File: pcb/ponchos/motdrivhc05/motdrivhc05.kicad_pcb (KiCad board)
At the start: 2 copper layers, 53.3 x 61.6 mm, 21 parts, among them J1 Screw_Terminal_1x06, J3 GW-040, J4 CONN_01X02, Q1 TIP31, U1 L293

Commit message: Agregado y modificado de nombres de nets en esquemático. Agregado de serigrafías con referencias en PCB.
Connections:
- net /M3A renamed /3A
- net /M4A renamed /4A
- net Net-(D2-Pad2) renamed /M1B
- net Net-(D4-Pad2) renamed /M2B
- net Net-(D9-Pad1) renamed /EXT
- D1 pad 2: Net-(D1-Pad2) -> /M1A
- D3 pad 2: Net-(D3-Pad2) -> /M2A
- D5 pad 1: Net-(D1-Pad2) -> /M1A
- D7 pad 1: Net-(D3-Pad2) -> /M2A
- J1 pad 4: Net-(D1-Pad2) -> /M1A
- J1 pad 6: Net-(D3-Pad2) -> /M2A
- SH1 pad 11: /M2A -> /2A
- SH1 pad 8: /M1A -> /1A
- U1 pad 11: Net-(D3-Pad2) -> /M2A
- U1 pad 2: /M1A -> /1A
- U1 pad 3: Net-(D1-Pad2) -> /M1A
- U1 pad 7: /M2A -> /2A
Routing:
- net /2A: track 0.00 -> 55.6 mm, vias 0 -> 2
- net /1A: track 0.00 -> 54.8 mm, vias 0 -> 2
- net Net-(D1-Pad2): track 46.9 -> 0.00 mm
- net Net-(D3-Pad2): track 38.7 -> 0.00 mm
- net /M2A: track 55.6 -> 38.7 mm, vias 2 -> 0
- net /M1A: track 54.8 -> 46.9 mm, vias 2 -> 0
- net GND: track 270.8 -> 270.1 mm
- net VCC: track 100.5 -> 100.0 mm
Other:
- board text added: "EXT"
- board text added: "GND"
- board text added: "M1A"
- board text added: "M1B"
- board text added: "M2A"
- board text added: "M2B"
- board text added: "NC"
- board text added: "VCC"

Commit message: Corregido error en disposición de pines de módulo bluetooth, y correción en PCB.
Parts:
- moved J3 12.7 mm to (66.7, 77.2)
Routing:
- net /BT_TXD: track 25.3 -> 39.3 mm
- net /BT_STATE: track 10.8 -> 20.6 mm
- net GND: track 270.1 -> 275.9 mm
- net +5V: track 165.9 -> 171.1 mm
- net Net-(J3-Pad2): track 7.27 -> 10.5 mm
- net /2A: track 55.6 -> 54.7 mm

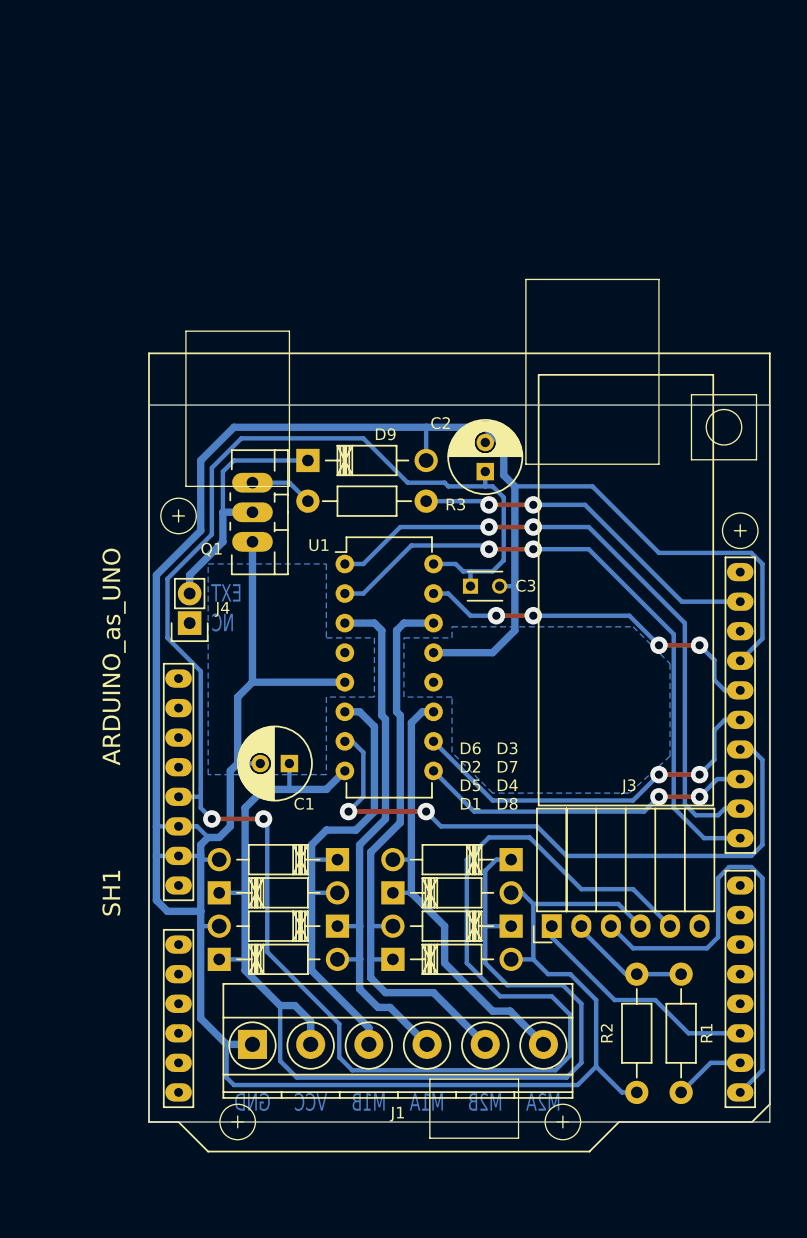
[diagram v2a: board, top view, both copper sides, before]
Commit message: Desplazadas pineras shield arduino. Agregado de serigrafía en capa cobre de datos de laboratorio y versión de la placa. Corregido 3D shape del conector de bluetooth.
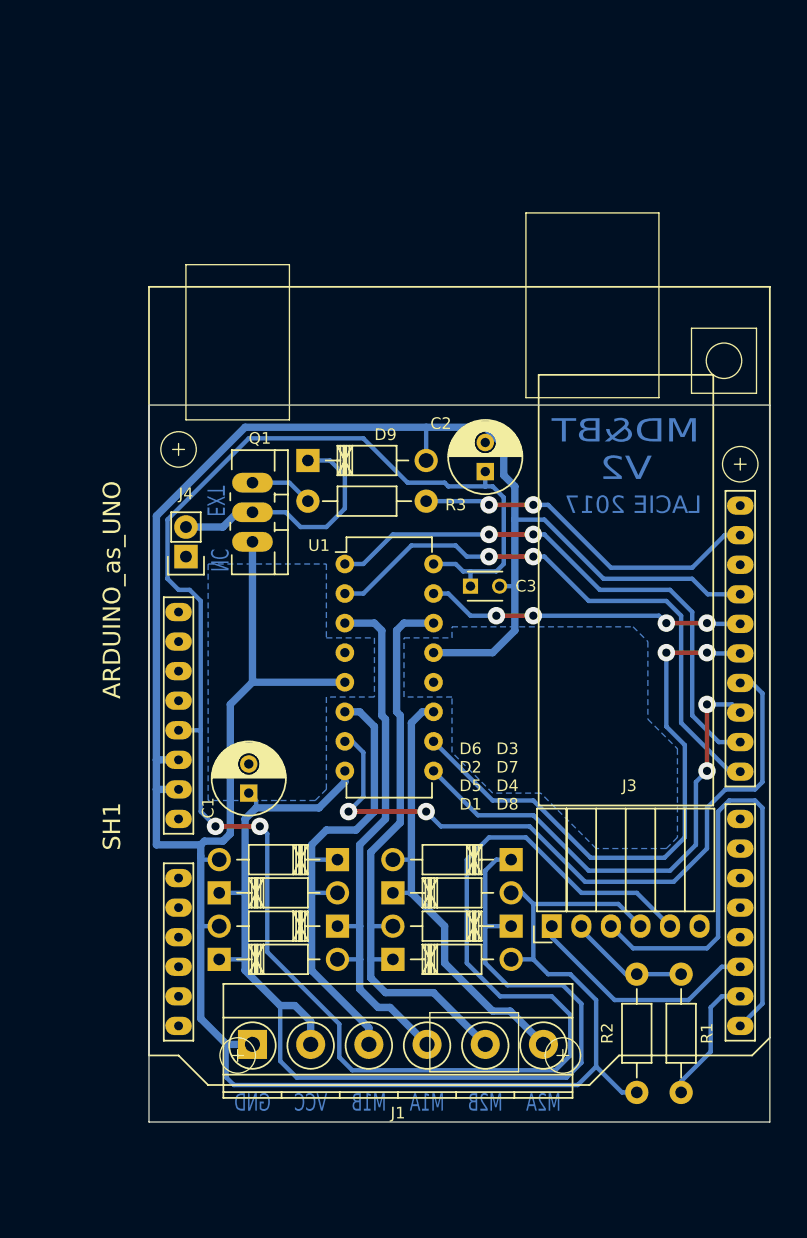
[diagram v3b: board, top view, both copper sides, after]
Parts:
- moved J4 5.72 mm to (35.2, 45.4)
- moved SH1 5.71 mm to (58.7, 56.5)
- moved C1 4.32 mm to (40.6, 65.7), turned to 90 degrees
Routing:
- net GND: track 275.9 -> 252.7 mm
- net /3A: track 32.8 -> 49.4 mm
- net /ME34: track 29.0 -> 42.6 mm
- net /ME12: track 54.9 -> 47.6 mm
- net /2A: track 54.7 -> 61.1 mm
- net /BT_TXD: track 39.3 -> 45.2 mm
- net /1A: track 54.8 -> 49.1 mm
- net /BT_RXD: track 6.13 -> 11.3 mm
- net /4A: track 30.8 -> 27.4 mm
- net VCC: track 100.0 -> 99.3 mm
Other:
- board text added: "LACIE 2017"
- board text added: "MD&BT V2"

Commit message: Algunas correciones varias. Desplazamiento del conector de motores, para que no interfieran las soldaduras con el conector SPI de arduino.
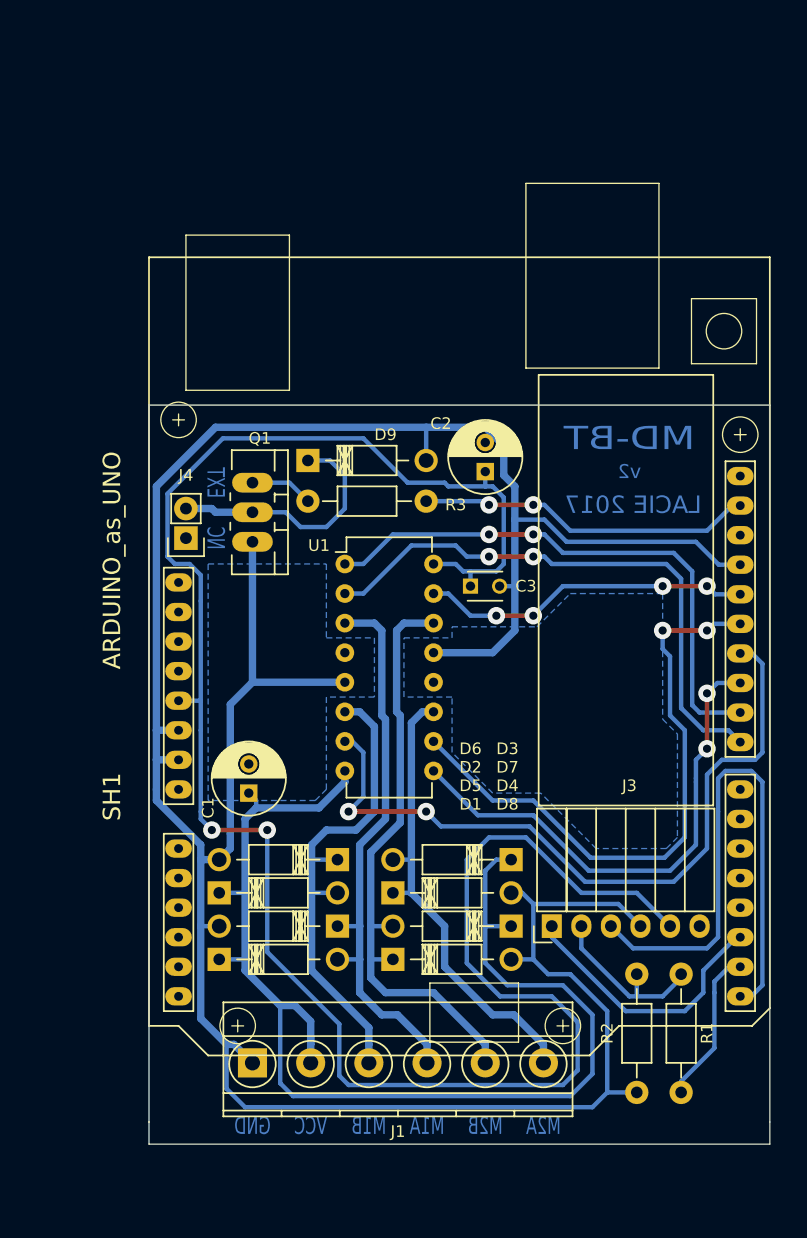
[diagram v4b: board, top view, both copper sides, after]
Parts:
- moved SH1 2.54 mm to (58.7, 54.0)
- moved J1 1.59 mm to (41.0, 88.9)
- moved J4 1.59 mm to (35.2, 43.8)
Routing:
- net VCC: track 99.3 -> 105.2 mm
- net +5V: track 171.1 -> 176.7 mm
- net Net-(J3-Pad2): track 10.5 -> 15.4 mm
- net /BT_TXD: track 45.2 -> 48.3 mm
- net /BT_STATE: track 20.6 -> 23.5 mm
- net /3A: track 49.4 -> 52.3 mm
- net /2A: track 61.1 -> 63.9 mm
- net /BT_RXD: track 11.3 -> 13.5 mm
- net /M1A: track 46.9 -> 48.6 mm
- net /M2A: track 38.7 -> 40.5 mm
- net /M2B: track 50.5 -> 52.1 mm
- net /M1B: track 40.6 -> 42.2 mm
- net /T1: track 30.5 -> 29.0 mm
- net /4A: track 27.4 -> 28.9 mm
- net GND: track 252.7 -> 253.8 mm
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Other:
- board size 53.3 x 61.6 mm -> 53.3 x 63.5 mm
- net class Default: via_dia 1 -> 1.5
- net class Motor: via_dia 1 -> 1.5
- board text added: "MD-BT"
- board text added: "v2"
- board text removed: "MD&BT V2"

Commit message: Corrimiento del conector, agujeros para disipador, giro capacitores para poner acostados, cambio pin del key/status, se quitó el transistor para rele.
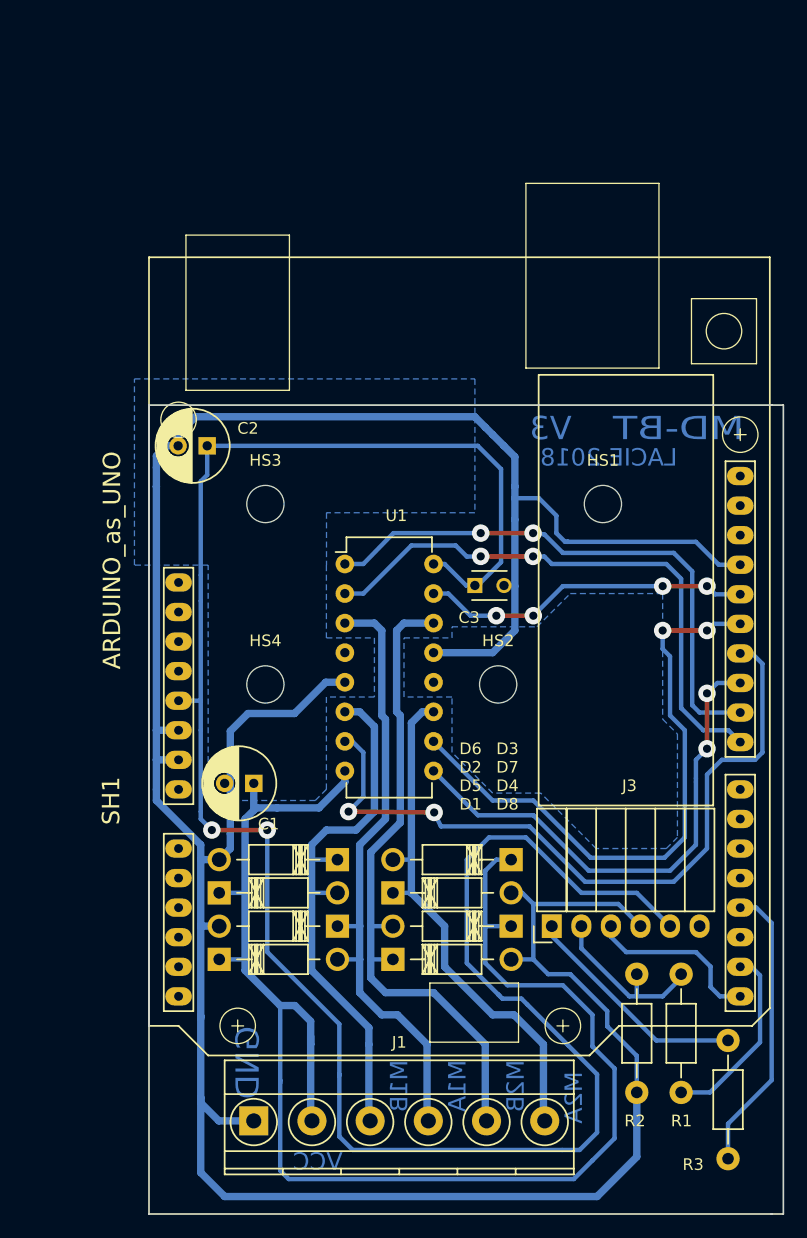
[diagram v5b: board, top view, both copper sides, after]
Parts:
- removed D9: 1N5819, Diodes_ThroughHole:Diode_DO-41_SOD81_Horizontal_RM10
- removed J4: CONN_01X02, Pin_Headers:Pin_Header_Straight_1x02
- removed Q1: TIP31, TO_SOT_Packages_THT:TO-220_Neutral123_Vertical_LargePads
- added HS1: Heatsink_PAD, Mounting_Holes:MountingHole_3.2mm_M3_ISO14580, F.Cu at (71.1, 40.9)
- added HS2: Heatsink_PAD, Mounting_Holes:MountingHole_3.2mm_M3_ISO14580, F.Cu at (62.1, 56.4)
- added HS3: Heatsink_PAD, Mounting_Holes:MountingHole_3.2mm_M3_ISO14580, F.Cu at (42.1, 40.9)
- added HS4: Heatsink_PAD, Mounting_Holes:MountingHole_3.2mm_M3_ISO14580, F.Cu at (42.1, 56.4)
- R3: value 1K -> 2K
- moved R3 67.0 mm to (81.8, 97.1), turned to 90 degrees
- moved C2 24.0 mm to (37.1, 35.9), turned to 180 degrees
- moved J1 4.99 mm to (41.1, 93.9)
- moved C1 0.94 mm to (41.1, 64.9), turned to 180 degrees
- moved C3 0.38 mm to (60.1, 47.9)
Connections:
- net /T2 renamed Net-(SH1-PadA5/2)
- J3 pad 1: /BT_STATE -> Net-(J3-Pad1)
- R3 pad 1: Net-(Q1-Pad1) -> /BT_STATE
- R3 pad 2: /T1 -> Net-(J3-Pad1)
- SH1 pad 2: /BT_STATE -> Net-(SH1-Pad2)
- SH1 pad 3: Net-(SH1-Pad3) -> /BT_STATE
- SH1 pad A4/2: /T1 -> Net-(SH1-PadA4/2)
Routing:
- net /BT_TXD: track 48.3 -> 15.2 mm
- net /T1: track 29.0 -> 0.00 mm, vias 2 -> 0
- net VCC: track 105.2 -> 127.8 mm
- net /EXT: track 21.5 -> 0.00 mm
- net Net-(J3-Pad1): track 0.00 -> 19.7 mm
- net +5V: track 176.7 -> 185.5 mm
- net GND: track 253.8 -> 261.2 mm
- net Net-(Q1-Pad1): track 5.42 -> 0.00 mm
- net /M2A: track 40.5 -> 45.5 mm
- net /M1A: track 48.6 -> 53.7 mm
- net /M1B: track 42.2 -> 47.2 mm
- net /M2B: track 52.1 -> 57.1 mm
- net /BT_RXD: track 13.5 -> 16.3 mm
- net /BT_STATE: track 23.5 -> 25.1 mm
- net Net-(SH1-PadA4/2): track 0.00 -> 0.76 mm
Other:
- board size 53.3 x 63.5 mm -> 54.5 x 69.5 mm
- board text added: "LACIE 2018"
- board text added: "V3"
- board text removed: "EXT"
- board text removed: "LACIE 2017"
- board text removed: "NC"
- board text removed: "v2"

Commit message: Subo el margen de 0,2 a 0,4 y corrijo algunas distancias. Faltan unas pocas más.
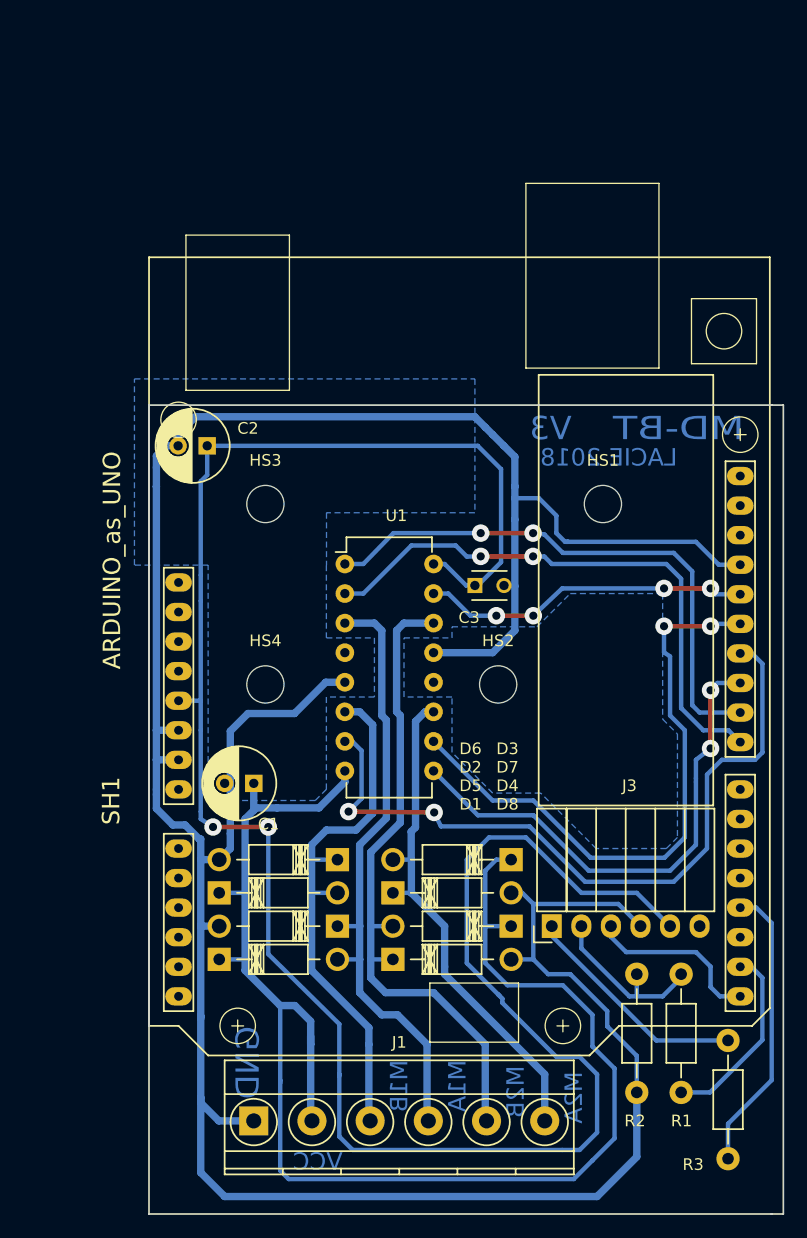
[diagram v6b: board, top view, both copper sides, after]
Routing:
- net /M2A: track 45.5 -> 44.7 mm
- net GND: track 261.2 -> 261.9 mm
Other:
- net class Default: clearance 0.2 -> 0.4
- net class Motor: clearance 0.2 -> 0.4
- rule trace_clearance: 0.2 -> 0.4

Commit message: Shield de motores plano, con mayor margen.
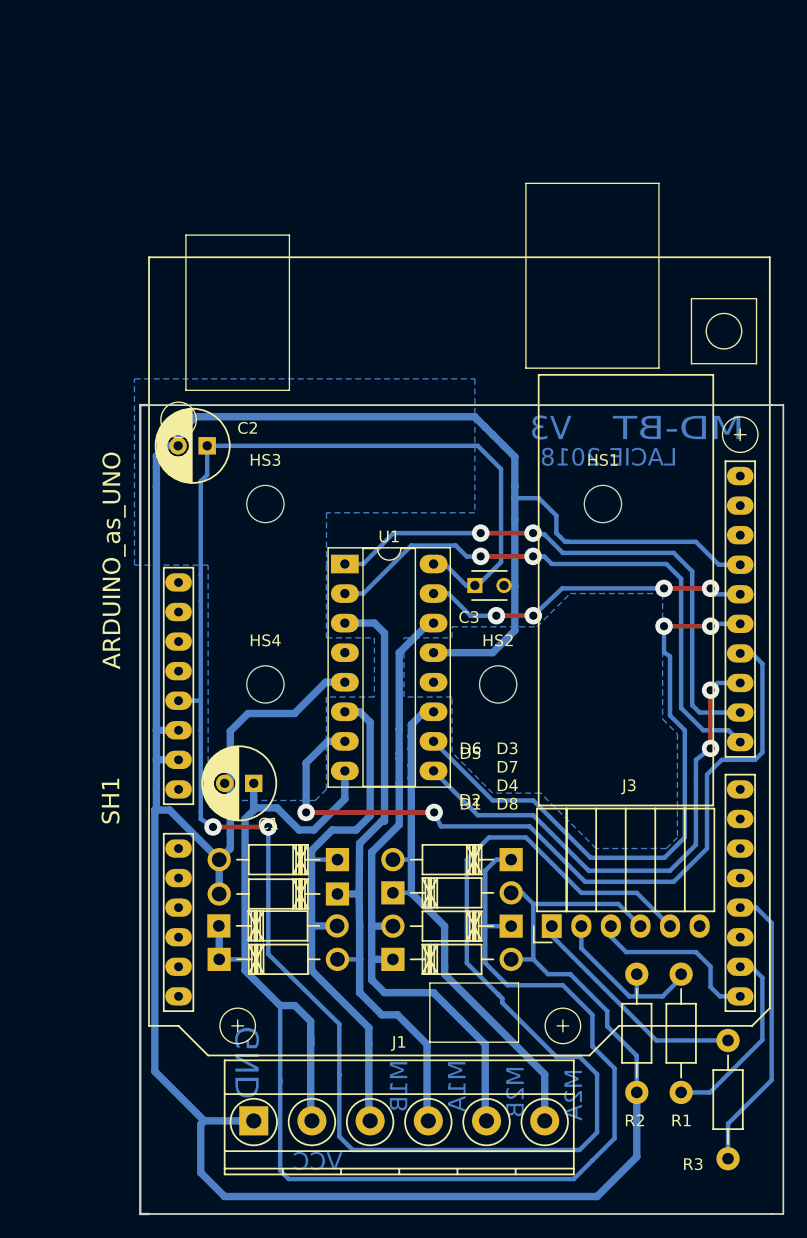
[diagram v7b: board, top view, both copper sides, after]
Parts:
- U1: footprint Housings_DIP:DIP-16_W7.62mm -> Package_DIP:DIP-16_W7.62mm_Socket_LongPads
- moved D2 2.84 mm to (38.1, 77.1)
- moved D5 2.76 mm to (48.3, 74.4)
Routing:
- net /2A: track 64.0 -> 69.1 mm
- net GND: track 261.9 -> 267.0 mm
- net VCC: track 127.8 -> 130.9 mm
- net /M2B: track 57.1 -> 55.5 mm
- net /M1B: track 47.1 -> 46.6 mm
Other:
- board size 54.5 x 69.5 mm -> 55.2 x 69.5 mm

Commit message: Se ensancharon algunas pistas.
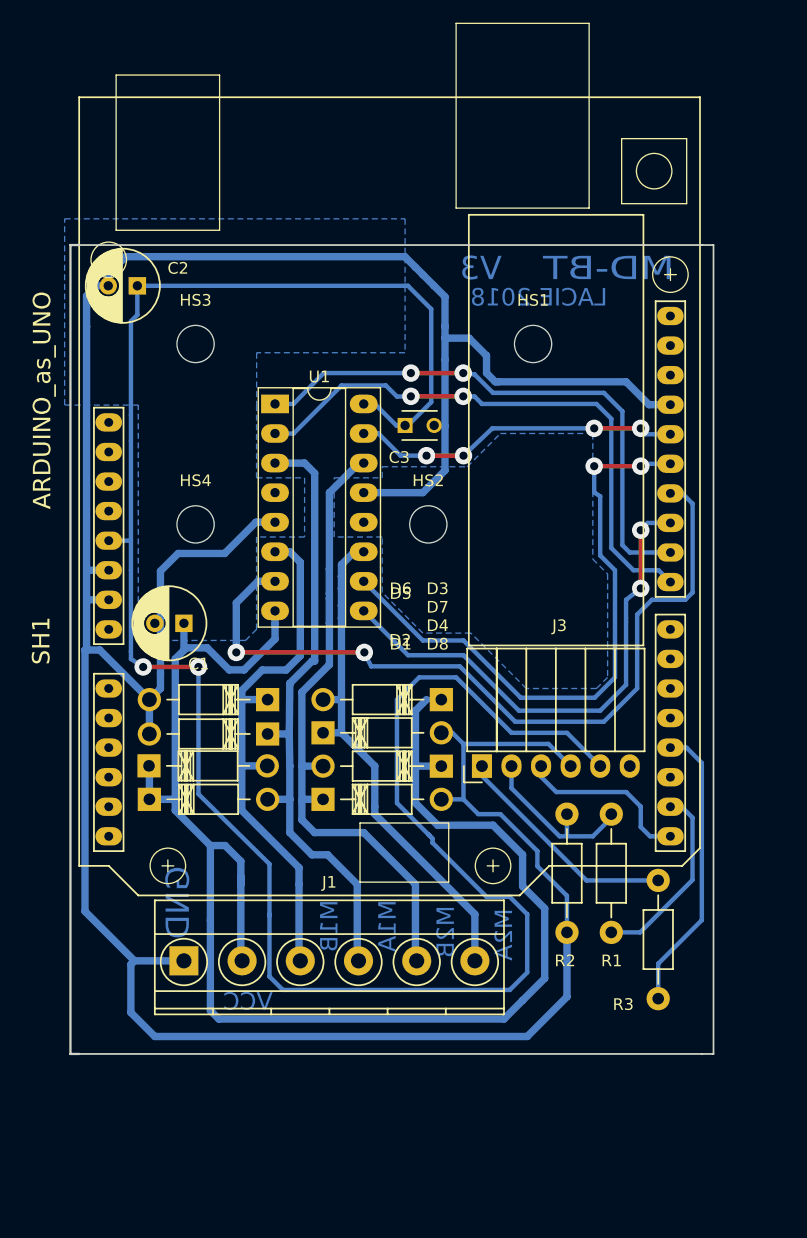
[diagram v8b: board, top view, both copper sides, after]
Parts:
- moved C1 15.0 mm to (35.1, 51.1)
- moved D2 15.0 mm to (32.1, 63.4)
- moved C2 15.0 mm to (31.1, 22.1)
- moved C3 15.0 mm to (54.1, 34.1)
- moved D1 15.0 mm to (32.1, 66.3)
- moved D3 15.0 mm to (57.2, 57.7)
- moved D4 15.0 mm to (57.2, 63.4)
- moved D5 15.0 mm to (42.3, 60.6)
- moved D6 15.0 mm to (42.3, 57.7)
- moved D7 15.0 mm to (47.0, 60.5)
- moved D8 15.0 mm to (47.0, 66.3)
- moved HS1 15.0 mm to (65.1, 27.1)
- moved HS2 15.0 mm to (56.1, 42.6)
- moved HS3 15.0 mm to (36.1, 27.1)
- moved HS4 15.0 mm to (36.1, 42.6)
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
